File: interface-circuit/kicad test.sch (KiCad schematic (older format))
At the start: 17 parts, among them J1 PumpSSR, J2 Probe, J3 GPIO, J4 Buzzer, J5 CoilSwitch, J6 FanPWR, J7 Rpi PWR, J8 PiScreen Power, J9 ATX PWR IN, Q1 2N3904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

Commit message: Debugging board revealed that the transistors on the PCB plan have reversed pin assignments. This commit fixes it.
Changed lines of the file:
@@
 	7350 2700 7400 2700
 Wire Wire Line
-	7700 2900 7700 3150
-Wire Wire Line
-	7700 3150 7700 3800
-Wire Wire Line
-	7700 3800 7700 4200
-Wire Wire Line
-	7700 4200 7700 5100
+	7700 2900 7700 5100
 Wire Wire Line
 	6650 3300 7050 3300
@@
 	7950 2400 7950 1450
 Wire Wire Line
-	7950 1450 8100 1450
-Wire Wire Line
-	8100 1450 8500 1450
-Wire Wire Line
-	8500 1450 9000 1450
+	7950 1450 9000 1450
 Text Label 6850 3500 0    60   ~ 0
 GPIO25
@@
 	8200 3050 8500 3050
 Wire Wire Line
-	7400 3150 7700 3150
-Wire Wire Line
-	7700 3150 8500 3150
+	7400 3150 8500 3150
 Connection ~ 7700 3150
 Wire Wire Line
-	9000 1450 9000 3450
-Wire Wire Line
-	9000 3450 9000 3700
+	9000 1450 9000 3700
 Connection ~ 9000 1450
 Wire Wire Line
-	7700 3800 8200 3800
-Wire Wire Line
-	8200 3800 8850 3800
-Wire Wire Line
-	8850 3800 9000 3800
+	7700 3800 9000 3800
 Connection ~ 7700 3800
 Wire Wire Line
@@
 Connection ~ 9000 3450
 Wire Wire Line
-	6650 4200 7700 4200
-Wire Wire Line
-	7700 4200 10000 4200
+	6650 4200 10000 4200
 Connection ~ 7700 4200
 $Comp
@@
 	6650 2500 6650 2600
 Wire Wire Line
-	4950 2500 5150 2500
-Wire Wire Line
-	5150 2500 6650 2500
+	4950 2500 6650 2500
 Text Label 5200 2500 0    60   ~ 0
 5V

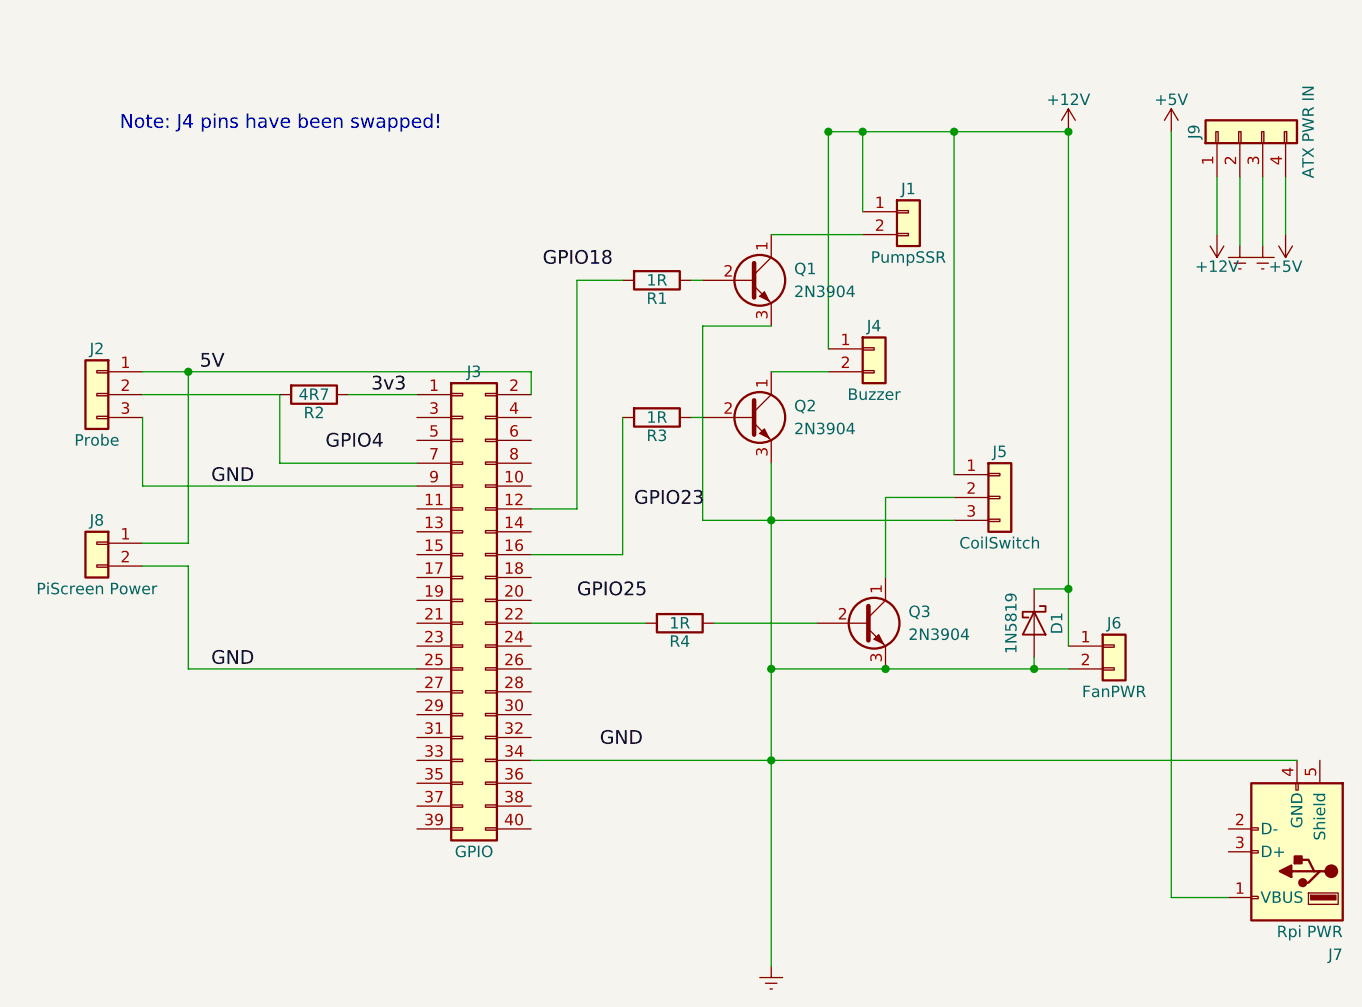
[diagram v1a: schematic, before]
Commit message: I corrected the issue with the J4 connector
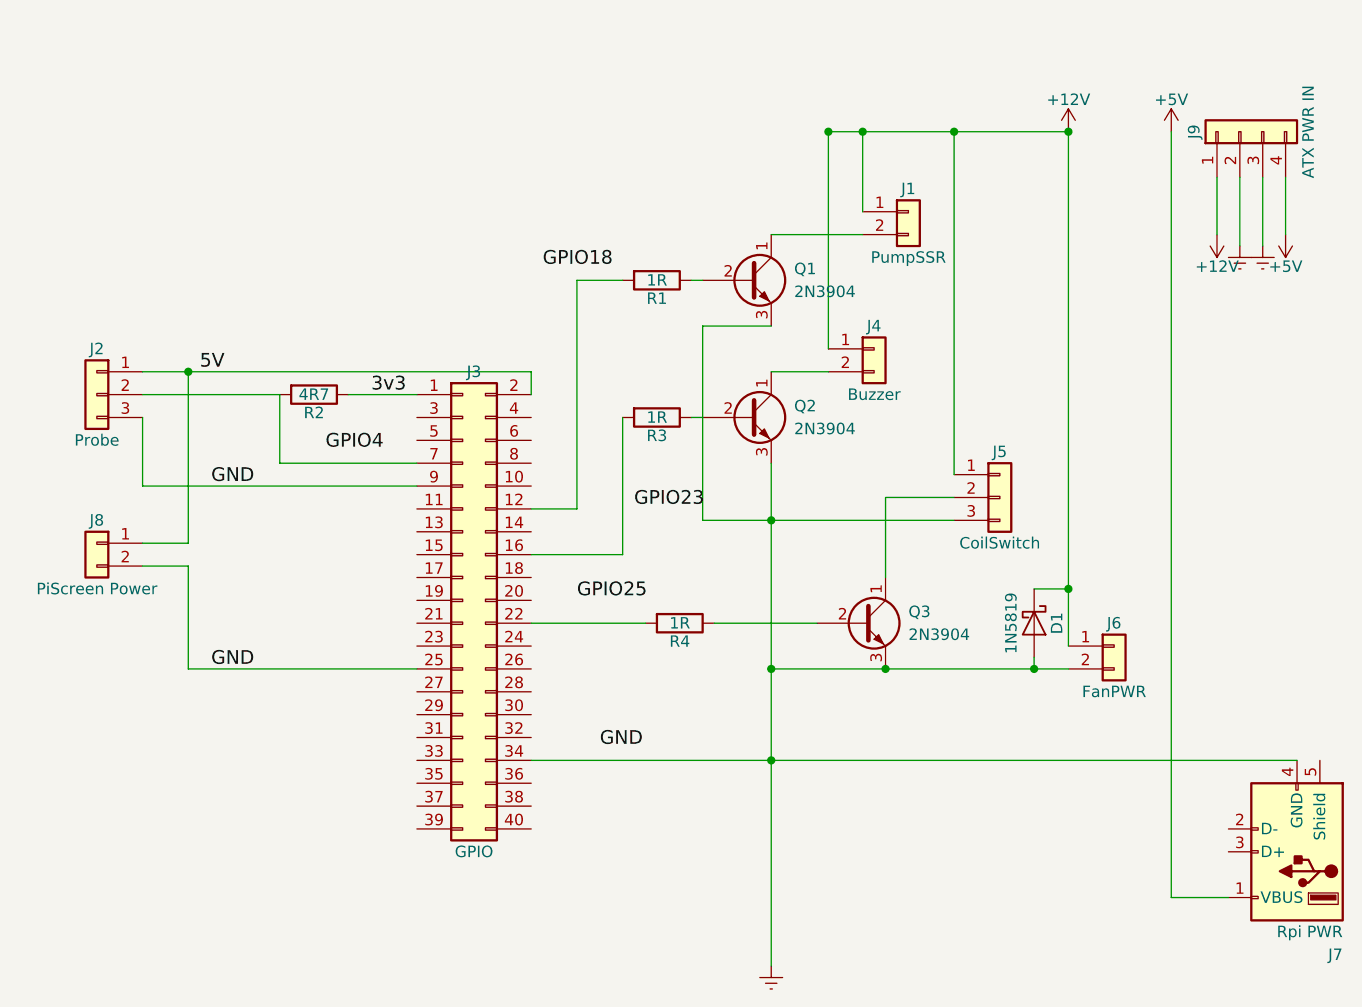
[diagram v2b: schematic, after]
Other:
- note removed: "Note: J4 pins have been swapped!"
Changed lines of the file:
@@
 	7350 2700 7400 2700
 Wire Wire Line
-	7700 2900 7700 5100
+	7700 2900 7700 3150
+Wire Wire Line
+	7700 3150 7700 3800
+Wire Wire Line
+	7700 3800 7700 4200
+Wire Wire Line
+	7700 4200 7700 5100
 Wire Wire Line
 	6650 3300 7050 3300
@@
 	7950 2400 7950 1450
 Wire Wire Line
-	7950 1450 9000 1450
+	7950 1450 8100 1450
+Wire Wire Line
+	8100 1450 8500 1450
+Wire Wire Line
+	8500 1450 9000 1450
 Text Label 6850 3500 0    60   ~ 0
 GPIO25
@@
 	8200 3050 8500 3050
 Wire Wire Line
-	7400 3150 8500 3150
+	7400 3150 7700 3150
+Wire Wire Line
+	7700 3150 8500 3150
 Connection ~ 7700 3150
 Wire Wire Line
-	9000 1450 9000 3700
+	9000 1450 9000 3450
+Wire Wire Line
+	9000 3450 9000 3700
 Connection ~ 9000 1450
 Wire Wire Line
-	7700 3800 9000 3800
+	7700 3800 8200 3800
+Wire Wire Line
+	8200 3800 8850 3800
+Wire Wire Line
+	8850 3800 9000 3800
 Connection ~ 7700 3800
 Wire Wire Line
@@
 Connection ~ 9000 3450
 Wire Wire Line
-	6650 4200 10000 4200
+	6650 4200 7700 4200
+Wire Wire Line
+	7700 4200 10000 4200
 Connection ~ 7700 4200
 $Comp
@@
 	6650 2500 6650 2600
 Wire Wire Line
-	4950 2500 6650 2500
+	4950 2500 5150 2500
+Wire Wire Line
+	5150 2500 6650 2500
 Text Label 5200 2500 0    60   ~ 0
 5V
@@
 Text Label 5250 3800 0    60   ~ 0
 GND
-Text Notes 4850 1450 0    60   ~ 0
-Note: J4 pins have been swapped!
 $EndSCHEMATC

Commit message: I found that the Pi could not sink enough power from the USB connection for both itself and the official screen, so I moved the screen's power connecter such that it is now driven directly by the PSU
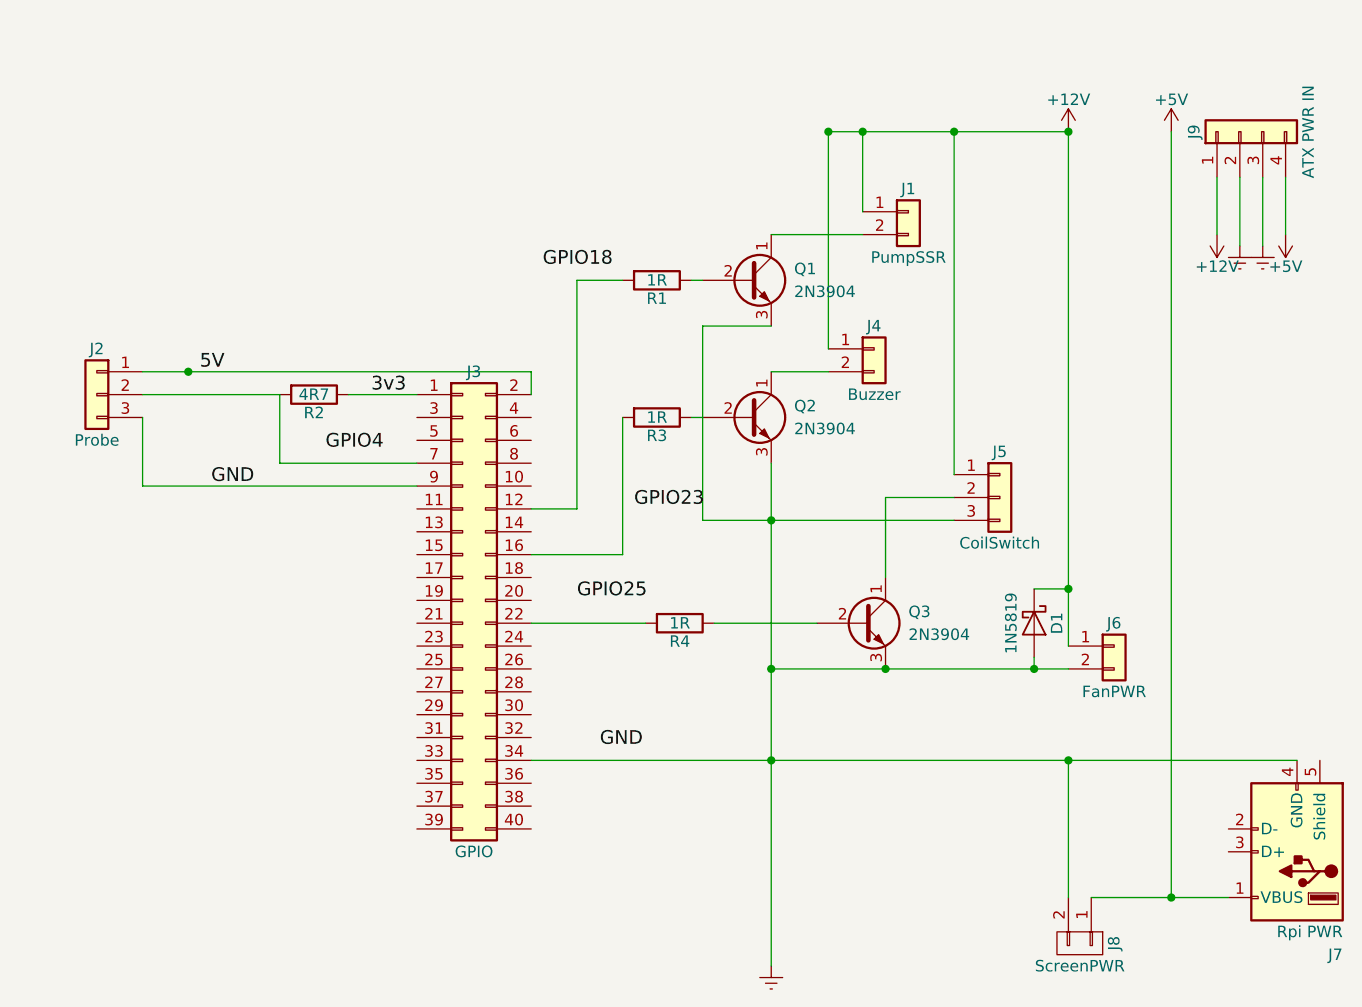
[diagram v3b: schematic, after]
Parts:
- removed J8: PiScreen Power, Pin_Headers:Pin_Header_Straight_1x02_Pitch2.54mm, symbol Conn_01x02
- added J8: ScreenPWR, Pin_Headers:Pin_Header_Straight_1x02_Pitch2.54mm_SMD_Pin1Right, symbol CONN_01X02
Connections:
- net +5V: now also J8.1 (P1)
- net Earth: now also J8.2 (P2)
- net GND: no longer J3.25 (Pin_25)
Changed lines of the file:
@@
 	7350 2700 7400 2700
 Wire Wire Line
-	7700 2900 7700 3150
-Wire Wire Line
-	7700 3150 7700 3800
-Wire Wire Line
-	7700 3800 7700 4200
-Wire Wire Line
-	7700 4200 7700 5100
+	7700 2900 7700 5100
 Wire Wire Line
 	6650 3300 7050 3300
@@
 	7950 2400 7950 1450
 Wire Wire Line
-	7950 1450 8100 1450
-Wire Wire Line
-	8100 1450 8500 1450
-Wire Wire Line
-	8500 1450 9000 1450
+	7950 1450 9000 1450
 Text Label 6850 3500 0    60   ~ 0
 GPIO25
@@
 	8200 3050 8500 3050
 Wire Wire Line
-	7400 3150 7700 3150
-Wire Wire Line
-	7700 3150 8500 3150
+	7400 3150 8500 3150
 Connection ~ 7700 3150
 Wire Wire Line
-	9000 1450 9000 3450
-Wire Wire Line
-	9000 3450 9000 3700
+	9000 1450 9000 3700
 Connection ~ 9000 1450
 Wire Wire Line
-	7700 3800 8200 3800
-Wire Wire Line
-	8200 3800 8850 3800
-Wire Wire Line
-	8850 3800 9000 3800
+	7700 3800 9000 3800
 Connection ~ 7700 3800
 Wire Wire Line
@@
 Connection ~ 9000 3450
 Wire Wire Line
-	6650 4200 7700 4200
-Wire Wire Line
-	7700 4200 10000 4200
+	6650 4200 10000 4200
 Connection ~ 7700 4200
-$Comp
-L Conn_01x02 J8
-U 1 1 5A8CE6B4
-P 4750 3250
-F 0 "J8" H 4750 3350 50  0000 C CNN
-F 1 "PiScreen Power" H 4750 3050 50  0000 C CNN
-F 2 "Pin_Headers:Pin_Header_Straight_1x02_Pitch2.54mm" H 4750 3250 50  0001 C CNN
-F 3 "" H 4750 3250 50  0001 C CNN
-	1    4750 3250
-	-1   0    0    -1
-$EndComp
 Text Label 6950 4150 0    60   ~ 0
 GND
@@
 	6650 2500 6650 2600
 Wire Wire Line
-	4950 2500 5150 2500
-Wire Wire Line
-	5150 2500 6650 2500
+	4950 2500 6650 2500
 Text Label 5200 2500 0    60   ~ 0
 5V
@@
 	7400 2300 7400 3150
 Wire Wire Line
-	9450 4800 9700 4800
+	9100 4800 9700 4800
 Wire Wire Line
 	7950 2500 7700 2500
@@
 Wire Wire Line
 	9450 1450 9450 4800
-Wire Wire Line
-	5150 2500 5150 3250
-Wire Wire Line
-	5150 3250 4950 3250
 Connection ~ 5150 2500
 Wire Wire Line
 	4950 3000 6150 3000
+$Comp
+L CONN_01X02 J8
+U 1 1 5A9D33AF
+P 9050 5000
+F 0 "J8" H 9050 5150 50  0000 C CNN
+F 1 "ScreenPWR" V 9150 5000 50  0000 C CNN
+F 2 "Pin_Headers:Pin_Header_Straight_1x02_Pitch2.54mm_SMD_Pin1Right" H 9050 5000 50  0001 C CNN
+F 3 "" H 9050 5000 50  0001 C CNN
+	1    9050 5000
+	0    1    1    0
+$EndComp
+Connection ~ 9450 4800
 Wire Wire Line
-	4950 3350 5150 3350
-Wire Wire Line
-	5150 3350 5150 3800
-Wire Wire Line
-	5150 3800 6150 3800
-Text Label 5250 3800 0    60   ~ 0
-GND
+	9000 4800 9000 4200
+Connection ~ 9000 4200
 $EndSCHEMATC
